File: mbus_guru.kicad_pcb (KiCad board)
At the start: 2 copper layers, 31.7 x 22.9 mm, 45 parts, among them J1 Conn_01x02, J2 Conn_01x02, J3 Conn_01x02, J4 Conn_01x03, Q1 BCV71, Q2 MMBT2907A, Q3 BCV71, Q4 MMBT2907A, Q5 BCV71, U1 74HC14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

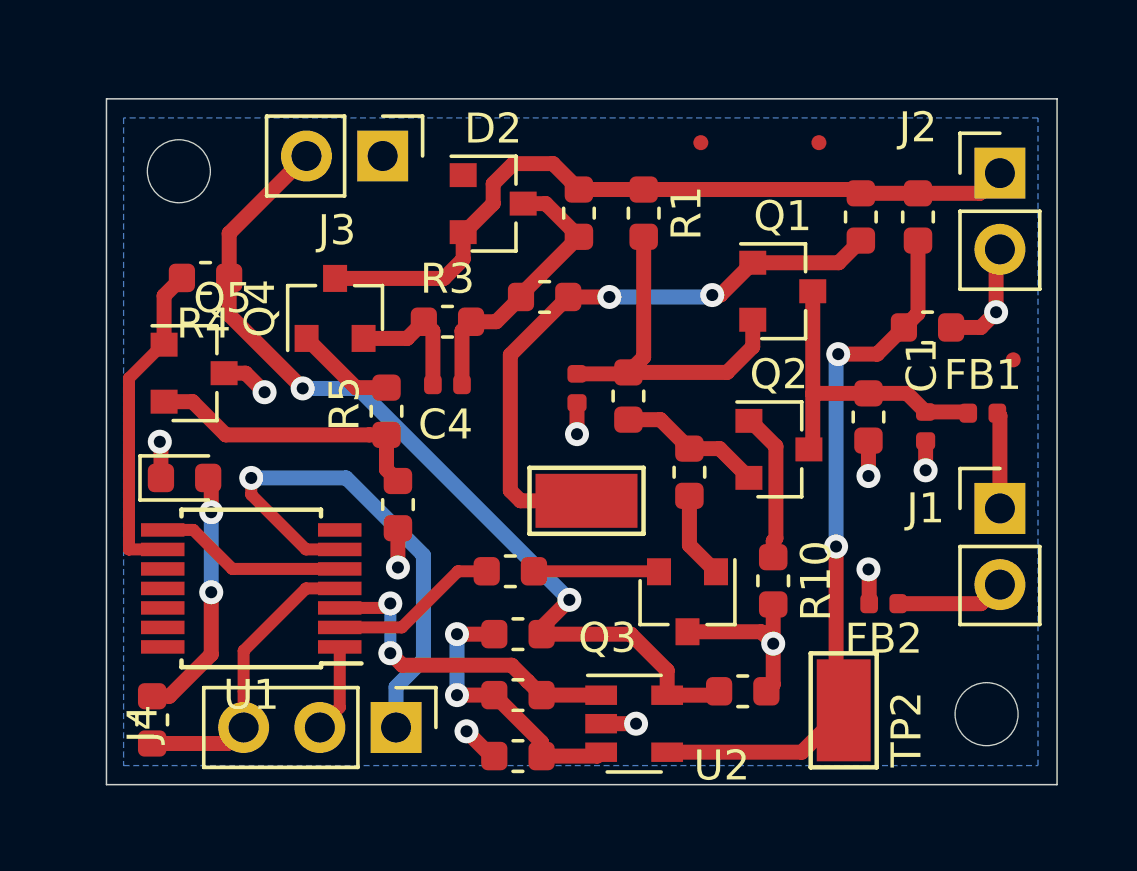
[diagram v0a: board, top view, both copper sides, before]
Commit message: Fixed bug with transistor footprints
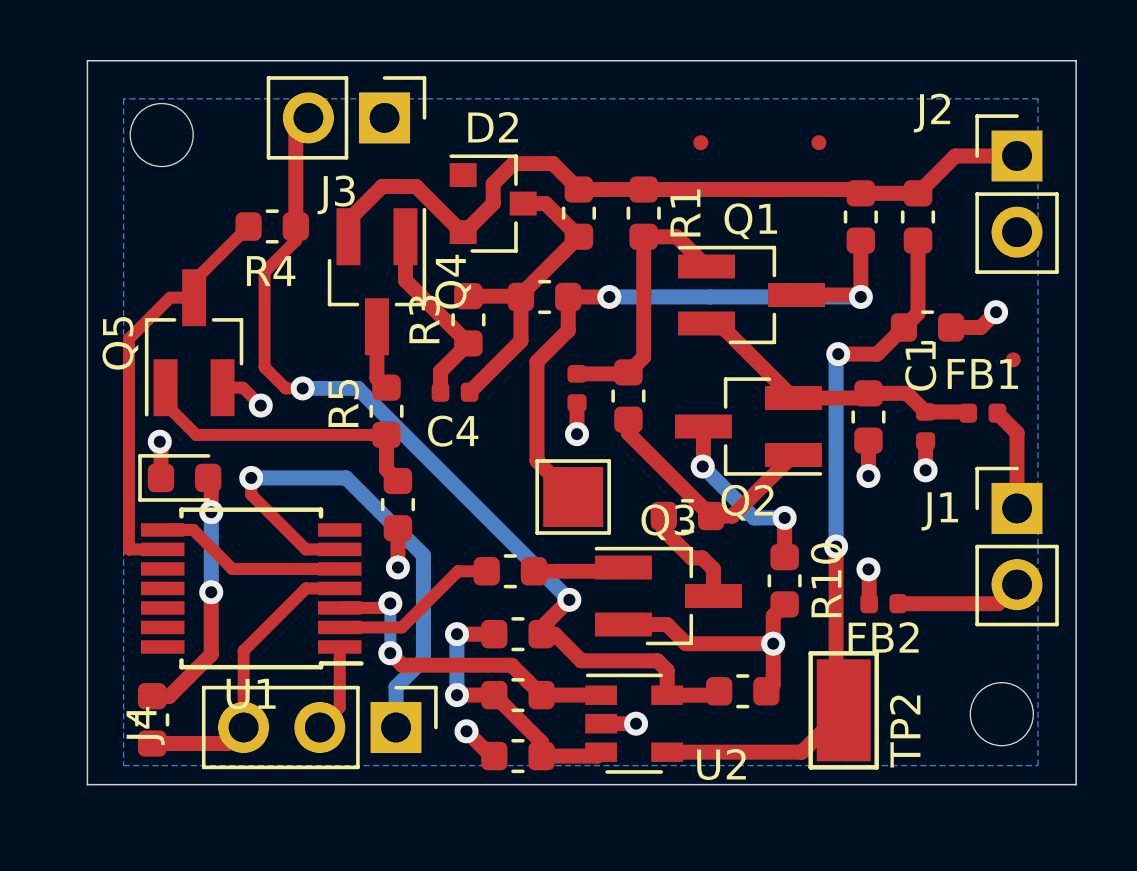
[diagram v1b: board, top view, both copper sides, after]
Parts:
- Q1, Q2, Q3, Q4, Q5: footprint Package_TO_SOT_SMD:SOT-23 -> SOT-23-Custom:BCV71_SOT-23_Handsoldering
- TP1: footprint TestPoint:TestPoint_Keystone_5015_Micro-Minature -> TestPoint:TestPoint_Pad_2.0x2.0mm
- moved R4 2.81 mm to (128.1, 83.6)
- moved Q4 1.66 mm to (131.6, 85.5), turned to 270 degrees
- moved R8 1.46 mm to (142.0, 93.3), turned to 180 degrees
- moved REF** 1.34 mm to (124.5, 80.6)
- moved J3 1.27 mm to (131.9, 80.0)
- moved Q2 1.27 mm to (144.0, 90.3), turned to 180 degrees
- moved Q1 1.05 mm to (144.1, 85.9)
- moved Q5 1.02 mm to (125.5, 87.5), turned to 90 degrees
- moved J2 0.81 mm to (153.0, 81.3)
- moved R3 0.70 mm to (134.7, 86.7), turned to 90 degrees
- moved Q3 0.66 mm to (141.4, 95.9), turned to 0 degrees
- moved J1 0.57 mm to (153.0, 93.0)
- moved REF** 0.51 mm to (152.5, 99.9)
- moved TP1 0.46 mm to (138.2, 92.6)
- moved R10 0.38 mm to (145.2, 95.4)
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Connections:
- net Net-(C1-Pad1) renamed /Q1E
- net Net-(C2-Pad1) renamed /Q1B
- net Net-(C3-Pad1) renamed /Q1C
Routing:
- net Net-(Q2-Pad2): track 4.85 -> 7.94 mm
- net Net-(Q5-Pad1): track 11.0 -> 14.0 mm
- net /Q1B: track 11.9 -> 8.97 mm
- net Net-(C4-Pad1): track 4.46 -> 7.05 mm
- net Net-(C3-Pad2): track 9.38 -> 10.8 mm
- net Net-(Q4-Pad1): track 3.34 -> 2.16 mm
- net Net-(Q3-Pad2): track 4.17 -> 3.03 mm
- net Net-(Q2-Pad1): track 4.98 -> 6.09 mm, vias 0 -> 2
- net /Q1C: track 20.5 -> 21.4 mm
- net /37V: track 25.5 -> 26.4 mm
- net /Q1E: track 10.8 -> 10.1 mm
- net Net-(Q3-Pad1): track 2.90 -> 3.56 mm
- net /3V3: track 30.6 -> 31.2 mm
- net /MBUS-N: track 3.65 -> 4.22 mm
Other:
- board size 31.7 x 22.9 mm -> 33 x 24.1 mm

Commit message: Added missing component U1G of 74HC14
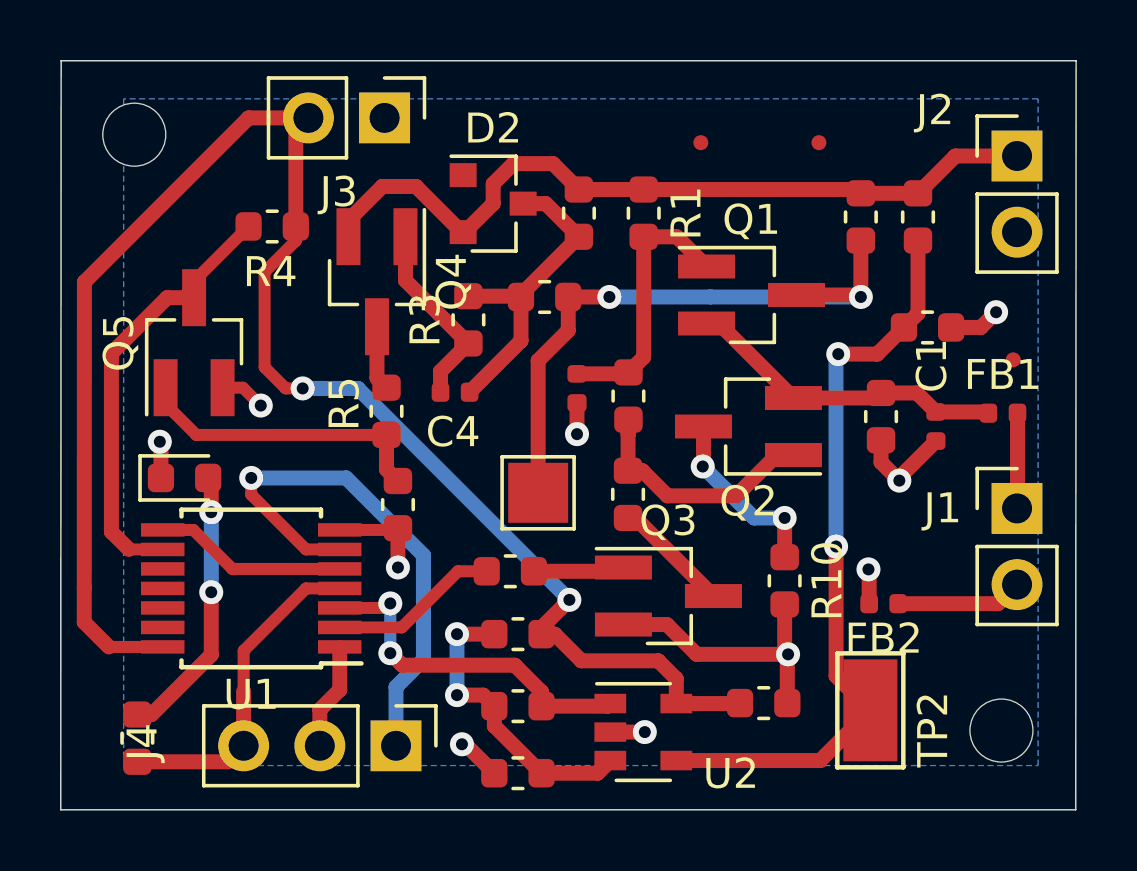
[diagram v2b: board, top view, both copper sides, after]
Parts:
- moved R8 2.11 mm to (140.0, 92.6), turned to 270 degrees
- moved TP1 1.18 mm to (137.0, 92.5)
- moved REF** 0.91 mm to (123.5, 80.6)
- moved TP2 0.89 mm to (148.1, 99.8)
- moved C5 0.80 mm to (144.5, 99.5)
- moved R18 0.79 mm to (123.6, 100.7)
- moved FB1 0.67 mm to (152.5, 89.9)
- moved J4 0.61 mm to (132.3, 100.9)
- moved R14 0.57 mm to (136.3, 101.9)
- moved REF** 0.55 mm to (152.5, 100.4)
- moved R9 0.42 mm to (148.4, 90.0)
- moved U2 0.41 mm to (140.5, 100.5)
- moved R15 0.37 mm to (136.3, 99.6)
- moved C1 0.34 mm to (150.3, 90.3)
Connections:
- net Net-(C4-Pad1) renamed /Q4B
- net Net-(Q2-Pad1) renamed /Q2C
- net Net-(Q2-Pad2) renamed /Q2B
- net Net-(Q3-Pad1) renamed /Q3C
- net Net-(Q3-Pad2) renamed /Q3B
- net Net-(Q4-Pad1) renamed /Q4C
- net Net-(Q5-Pad1) renamed /Q5C
- net Net-(Q5-Pad2) renamed /Q5B
- U1 pad 14: (no net) -> /3V3
- U1 pad 7: (no net) -> GND
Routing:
- net /3V3: track 31.2 -> 56.0 mm
- net GND: track 21.1 -> 25.3 mm, vias 11 -> 10
- net /MBUS-FAULT: track 9.89 -> 11.0 mm
- net Net-(R16-Pad2): track 24.1 -> 25.2 mm
- net Net-(R13-Pad2): track 9.29 -> 10.1 mm
- net Net-(R15-Pad2): track 11.0 -> 11.8 mm
- net Net-(D3-Pad2): track 8.47 -> 9.23 mm
- net /Q1E: track 10.1 -> 10.8 mm
- net /Q1C: track 21.4 -> 20.7 mm
- net /MBUS-TX: track 2.96 -> 3.55 mm
- net /Q5C: track 14.0 -> 14.6 mm
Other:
- board size 33 x 24.1 mm -> 33.8 x 25 mm
